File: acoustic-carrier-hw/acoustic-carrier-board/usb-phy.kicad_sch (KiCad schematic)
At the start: 76 parts, among them J9 TYPE-C-31-M-12, U18 LMV321, U6 TS3USB30EDGSR, U7 USB3300-EZK, Y3 Crystal_GND24_Small

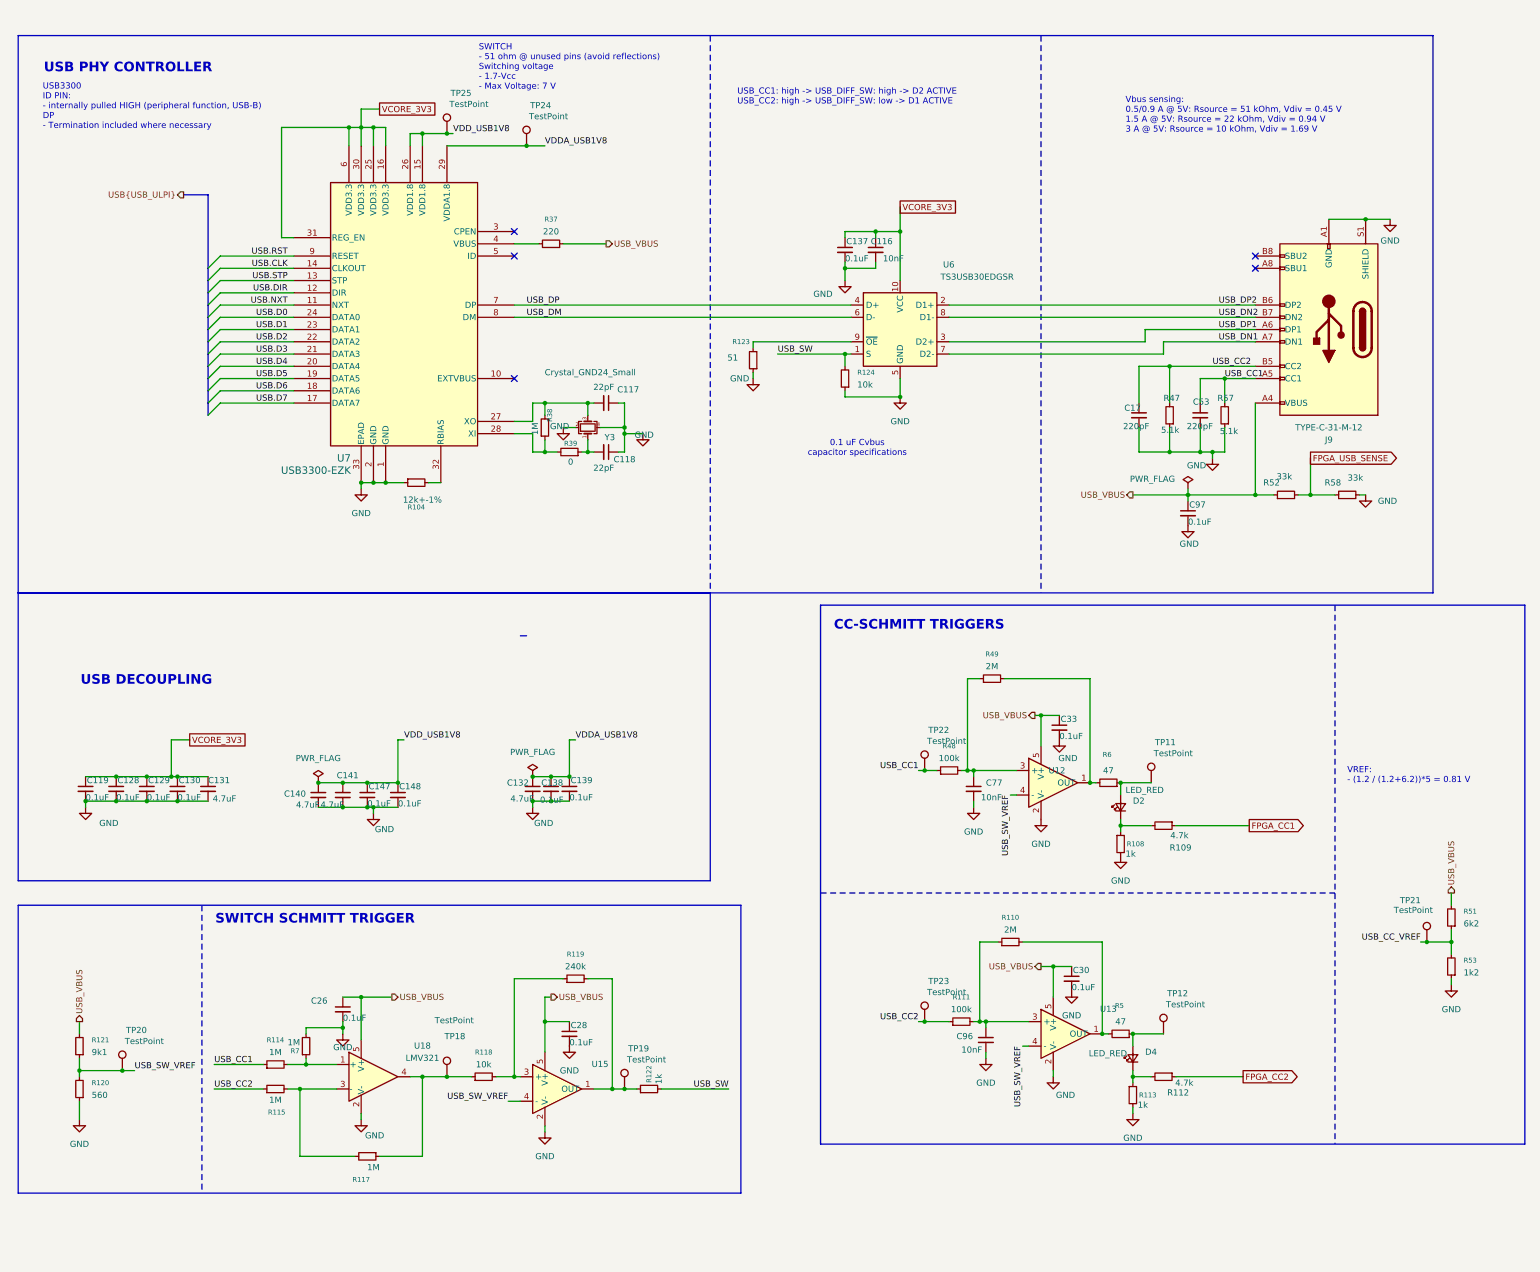
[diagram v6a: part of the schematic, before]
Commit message: [carrier] Finished rough layout, p (put together according to component category
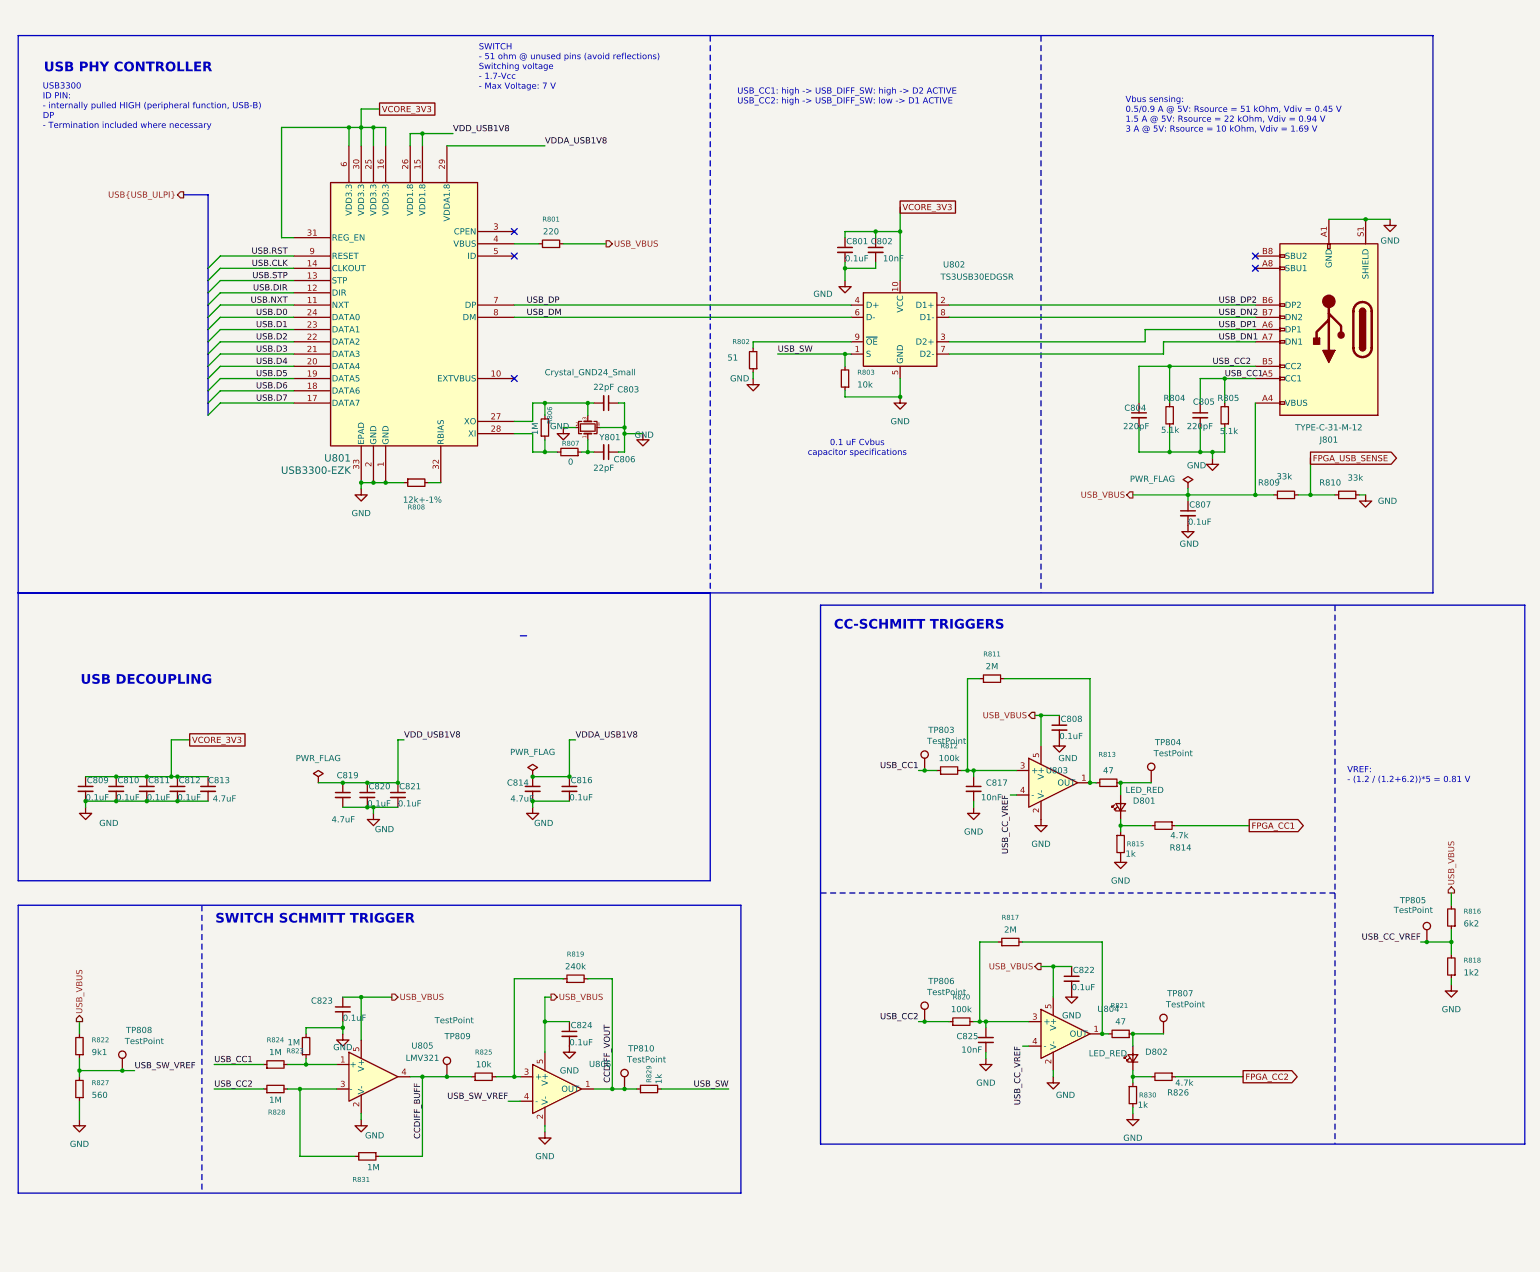
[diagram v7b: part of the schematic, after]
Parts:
- removed C138: 0.1uF, Capacitor_SMD:C_0402_1005Metric, symbol Device:C_Small
- removed C140: 4.7uF, Capacitor_SMD:C_0402_1005Metric, symbol Device:C_Small
- removed TP24, TP25: TestPoint, TestPoint:TestPoint_Loop_D1.80mm_Drill1.0mm_Beaded, symbol Connector:TestPoint
- renumbered C137 to C801, C116 to C802, C117 to C803, C17 to C804, C53 to C805, C118 to C806, C97 to C807, C33 to C808, C119 to C809, C128 to C810, C129 to C811, C130 to C812, C131 to C813, C132 to C814, C139 to C816, C77 to C817, C141 to C819, C147 to C820, C148 to C821, C30 to C822, C26 to C823, C28 to C824, C96 to C825, D2 to D801, D4 to D802, J9 to J801, R37 to R801, R123 to R802, R124 to R803, R47 to R804, R57 to R805, R38 to R806, R39 to R807, R104 to R808, R52 to R809, R58 to R810, R49 to R811, R48 to R812, R6 to R813, R109 to R814, R108 to R815, R51 to R816, R110 to R817, R53 to R818, R119 to R819, R111 to R820, R5 to R821, R121 to R822, R7 to R823, R114 to R824, R118 to R825, R112 to R826, R120 to R827, R115 to R828, R122 to R829, R113 to R830, R117 to R831, TP22 to TP803, TP11 to TP804, TP21 to TP805, TP23 to TP806, TP12 to TP807, TP20 to TP808, TP18 to TP809, TP19 to TP810, U7 to U801, U6 to U802, U12 to U803, U13 to U804, U18 to U805, U15 to U806, Y3 to Y801
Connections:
- net USB_CC_VREF: now also U803.4 (-), U804.4 (-)
- net USB_SW_VREF: no longer U803.4 (-), U804.4 (-)
- net CCDIFF_BUFF: now reaches R825.1, R831.1, TP809.1, U805.4
- net CCDIFF_VOUT: now reaches R819.2, R829.1, TP810.1, U806.1 (OUT)

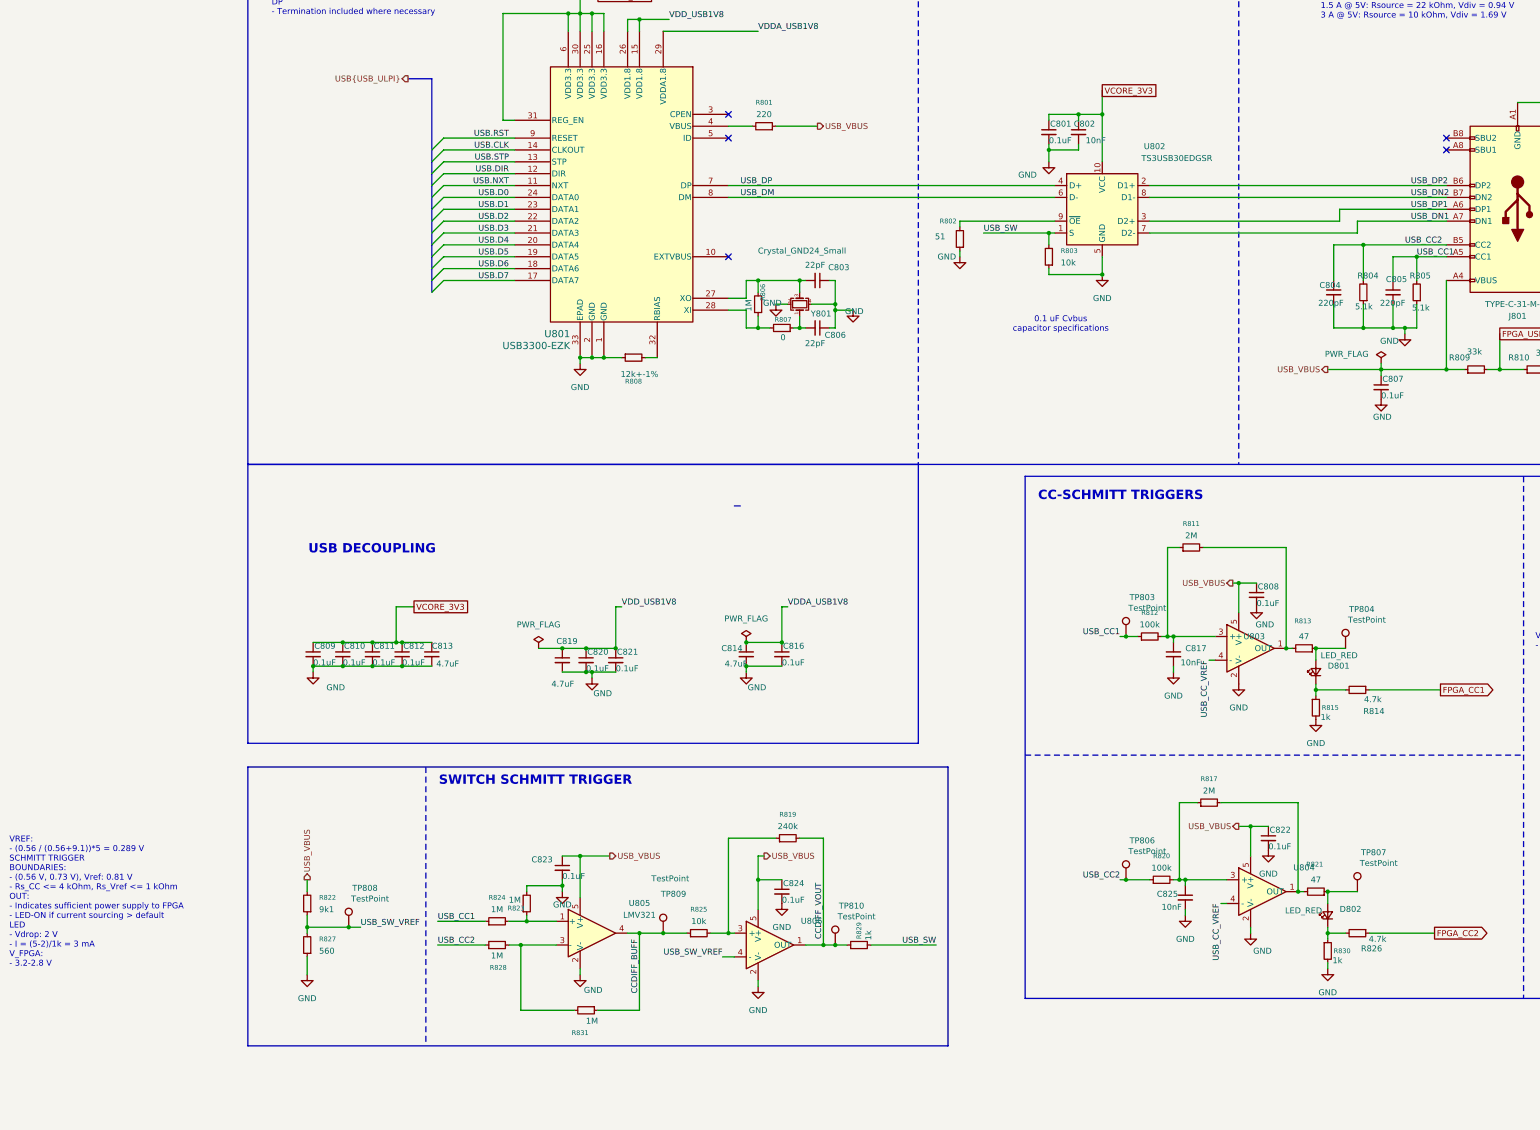
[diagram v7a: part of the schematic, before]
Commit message: [carrier] Removed USB-switch, placed decouplpling for DDR3 and ECP5U (next) consider adding buffers on CC1 and CC2 pins
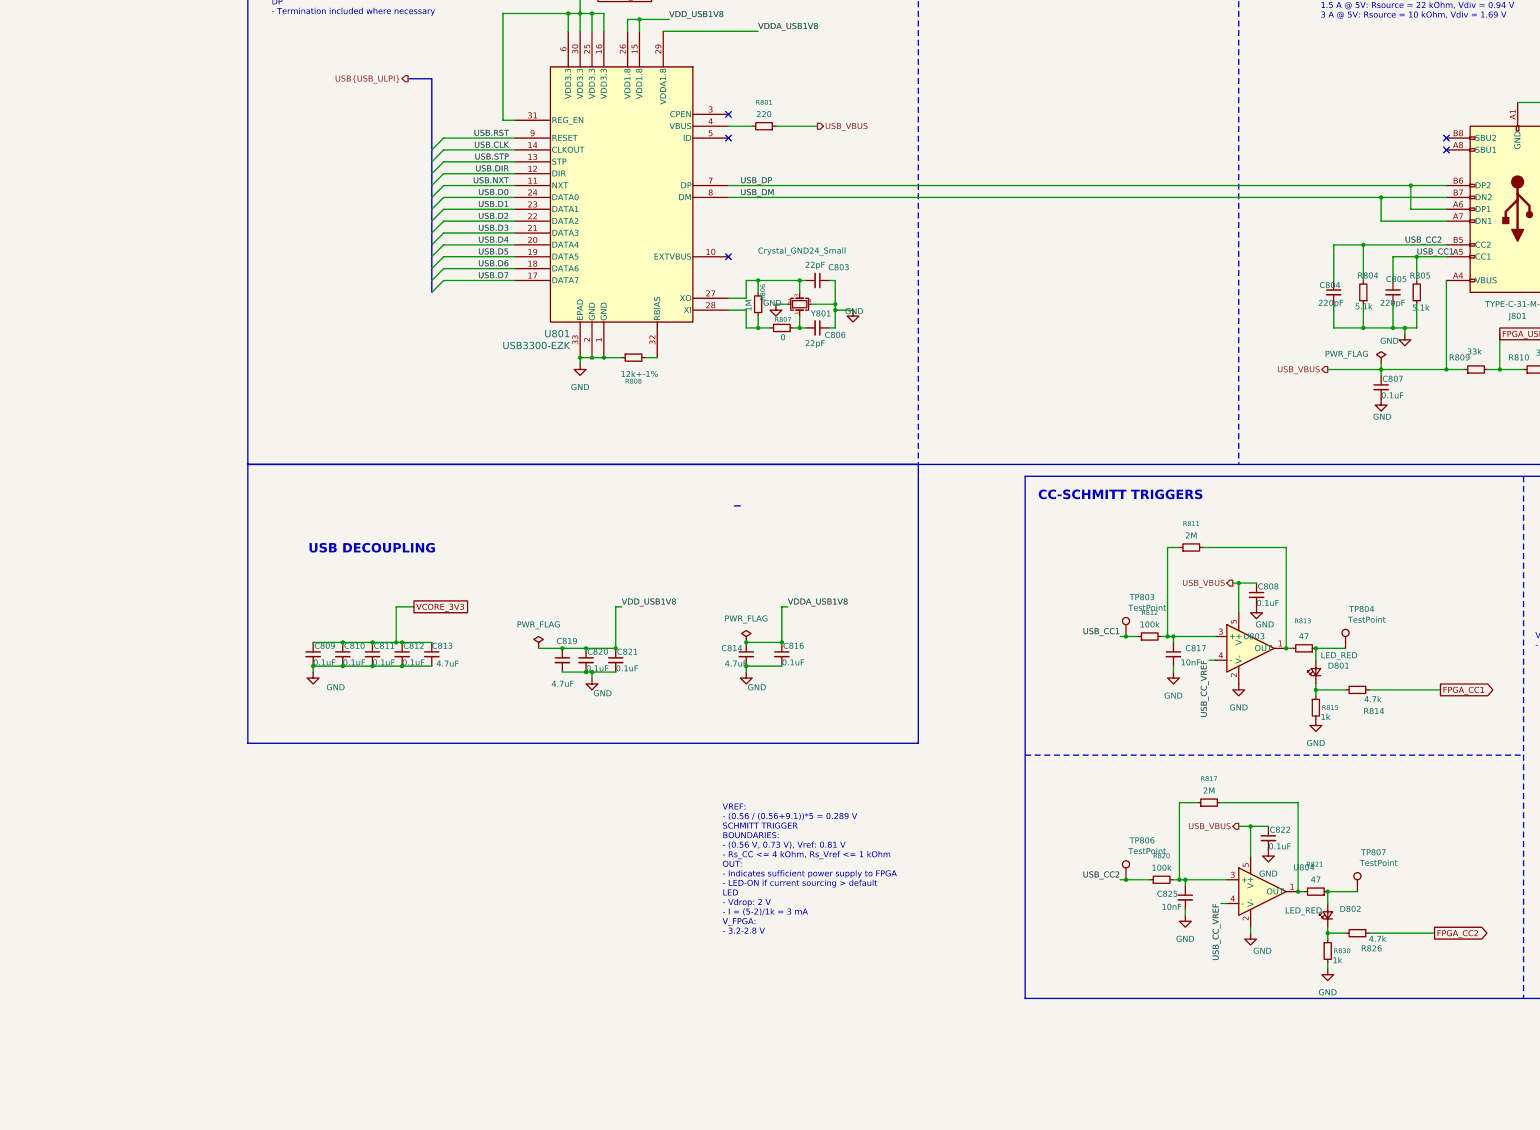
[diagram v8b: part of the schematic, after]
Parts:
- removed C801, C823, C824: 0.1uF, Capacitor_SMD:C_0402_1005Metric, symbol Device:C_Small
- removed C802: 10nF, Capacitor_SMD:C_0402_1005Metric, symbol Device:C_Small
- removed R802: 51, Resistor_SMD:R_0603_1608Metric, symbol Device:R_Small
- removed R803, R825: 10k, Resistor_SMD:R_0603_1608Metric, symbol Device:R_Small
- removed R819: 240k, Resistor_SMD:R_0603_1608Metric, symbol Device:R_Small
- removed R822: 9k1, Resistor_SMD:R_0603_1608Metric_Pad0.98x0.95mm_HandSolder, symbol Device:R_Small
- removed R823, R824, R828, R831: 1M, Resistor_SMD:R_0603_1608Metric_Pad0.98x0.95mm_HandSolder, symbol Device:R_Small
- removed R827: 560, Resistor_SMD:R_0603_1608Metric_Pad0.98x0.95mm_HandSolder, symbol Device:R_Small
- removed R829: 1k, Resistor_SMD:R_0603_1608Metric, symbol Device:R_Small
- removed TP808, TP809, TP810: TestPoint, TestPoint:TestPoint_Loop_D1.80mm_Drill1.0mm_Beaded, symbol Connector:TestPoint
- removed U802: TS3USB30EDGSR, Package_SO:VSSOP-10_3x3mm_P0.5mm, symbol Interface_USB:TS3USB30EDGSR
- removed U805: LMV321, Package_TO_SOT_SMD:SOT-23-5, symbol Amplifier_Operational:LMV321
- removed U806: ~, Package_TO_SOT_SMD:SOT-23-5, symbol iw-analog:COS3201
- C807, C808, C809, C810, C811, C812, C816, C820, C821, C822: footprint Capacitor_SMD:C_0402_1005Metric -> Capacitor_SMD:C_0201_0603Metric; LPN C307331 -> C22435929; MPN CL05B104KB54PNC -> CGA0201X7R104K160ET
- C817, C825: footprint Capacitor_SMD:C_0402_1005Metric -> Capacitor_SMD:C_0201_0603Metric; LPN C15195 -> C285010; MPN CL05B103KB5NNNC -> 0201B103K250NT
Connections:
- net USB_DN1 is gone; now on net USB_DM: J801.A7 (DN1)
- net USB_DN2 is gone; now on net USB_DM: J801.B7 (DN2)
- net USB_DP1 is gone; now on net USB_DP: J801.A6 (DP1)
- net USB_DP2 is gone; now on net USB_DP: J801.B6 (DP2)
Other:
- note removed: "0.1 uF Cvbus capacitor specifications"
